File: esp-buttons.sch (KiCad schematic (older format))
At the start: 35 parts, among them Q1 FDV304P, U1 ESP-07v2, U2 LD1117S33CTR

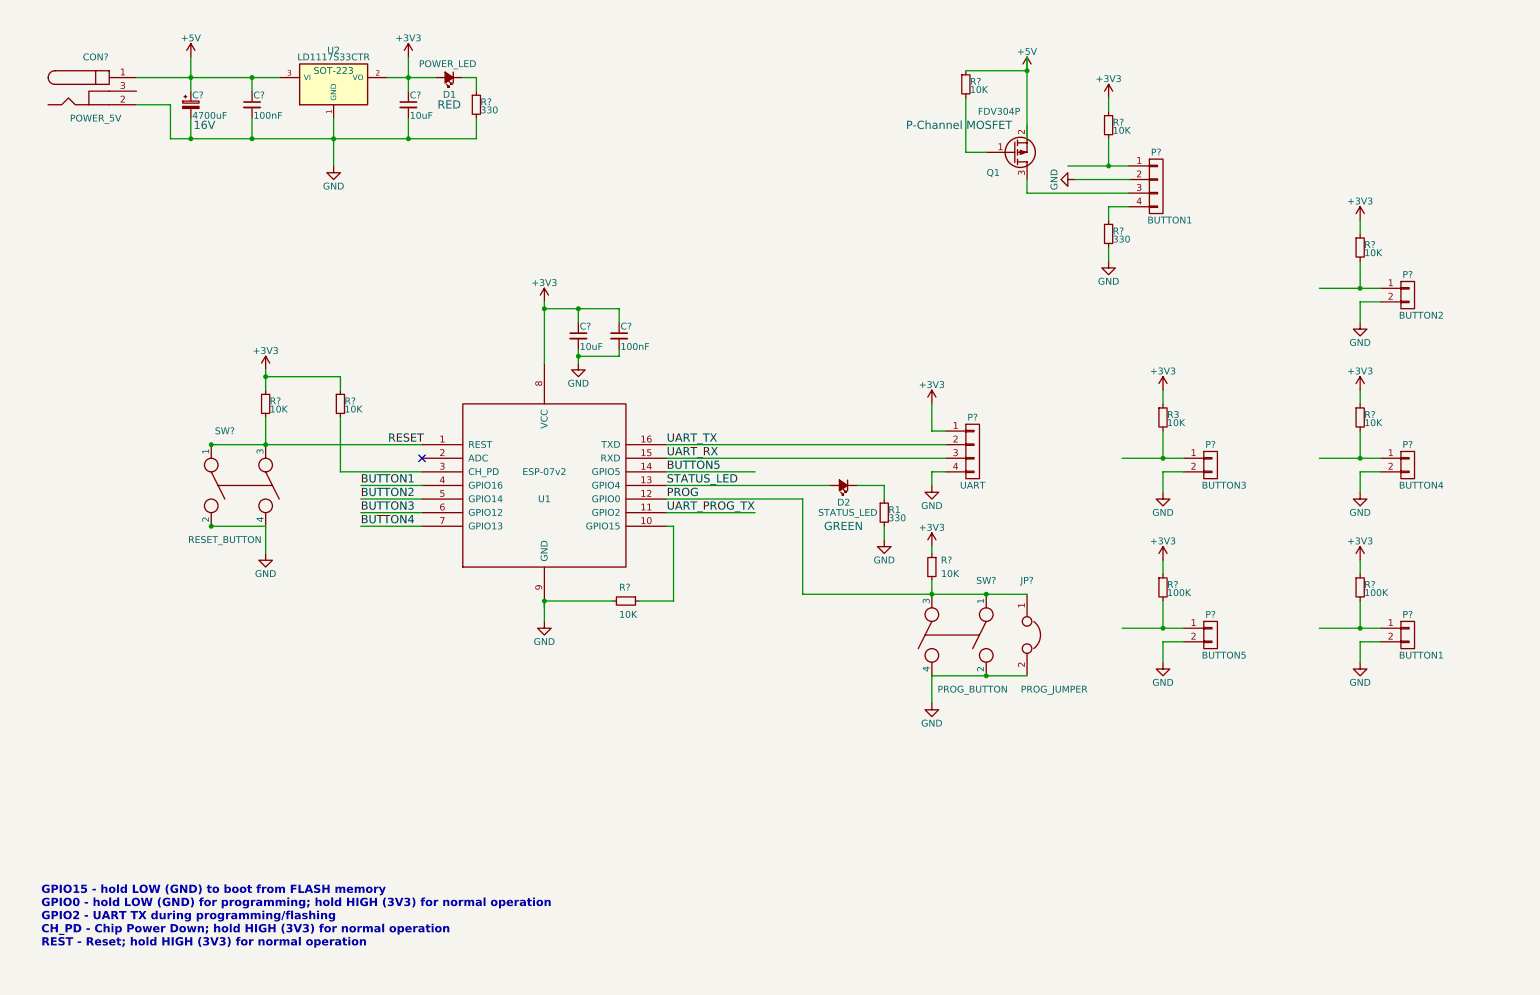
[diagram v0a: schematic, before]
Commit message: Removed one extra button circuitry
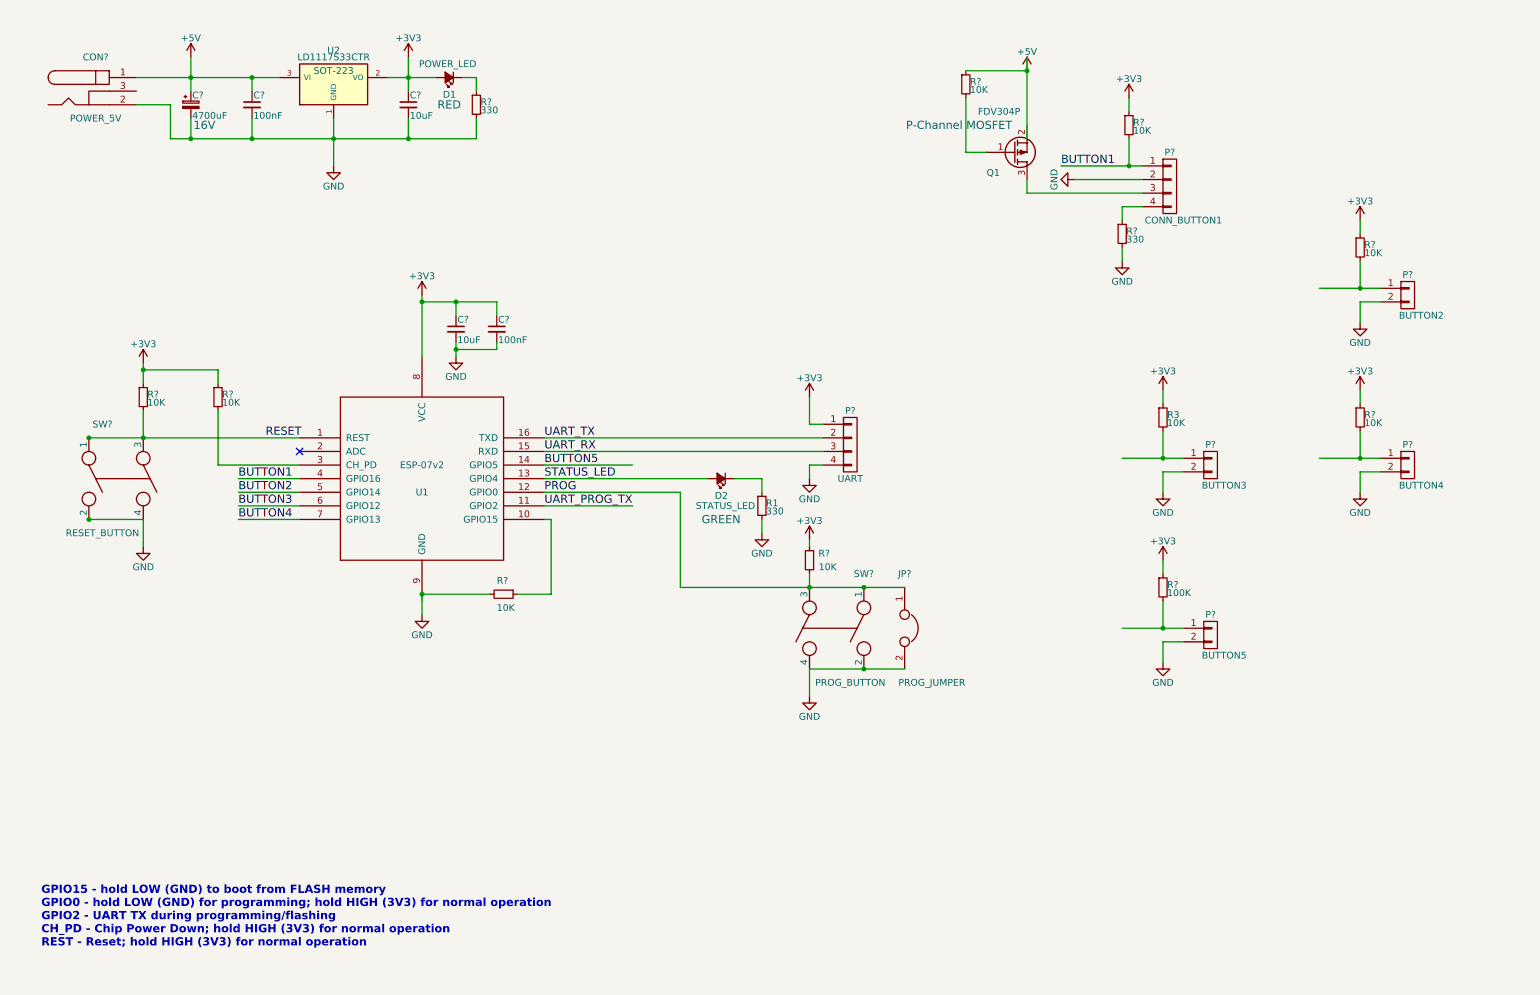
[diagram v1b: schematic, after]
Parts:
- removed P?: BUTTON1, symbol CONN_01X02
- removed R?: 100K, Resistors_SMD:R_1206_HandSoldering, symbol R_Small
- P?: value BUTTON1 -> CONN_BUTTON1
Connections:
- wire segments 98 -> 93
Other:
- moved on the sheet: C?, D2, JP?, P?, R1, R?, SW?, U1

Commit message: Minor modification to the POWER LED. Removed from repository the files that are in .gitignore
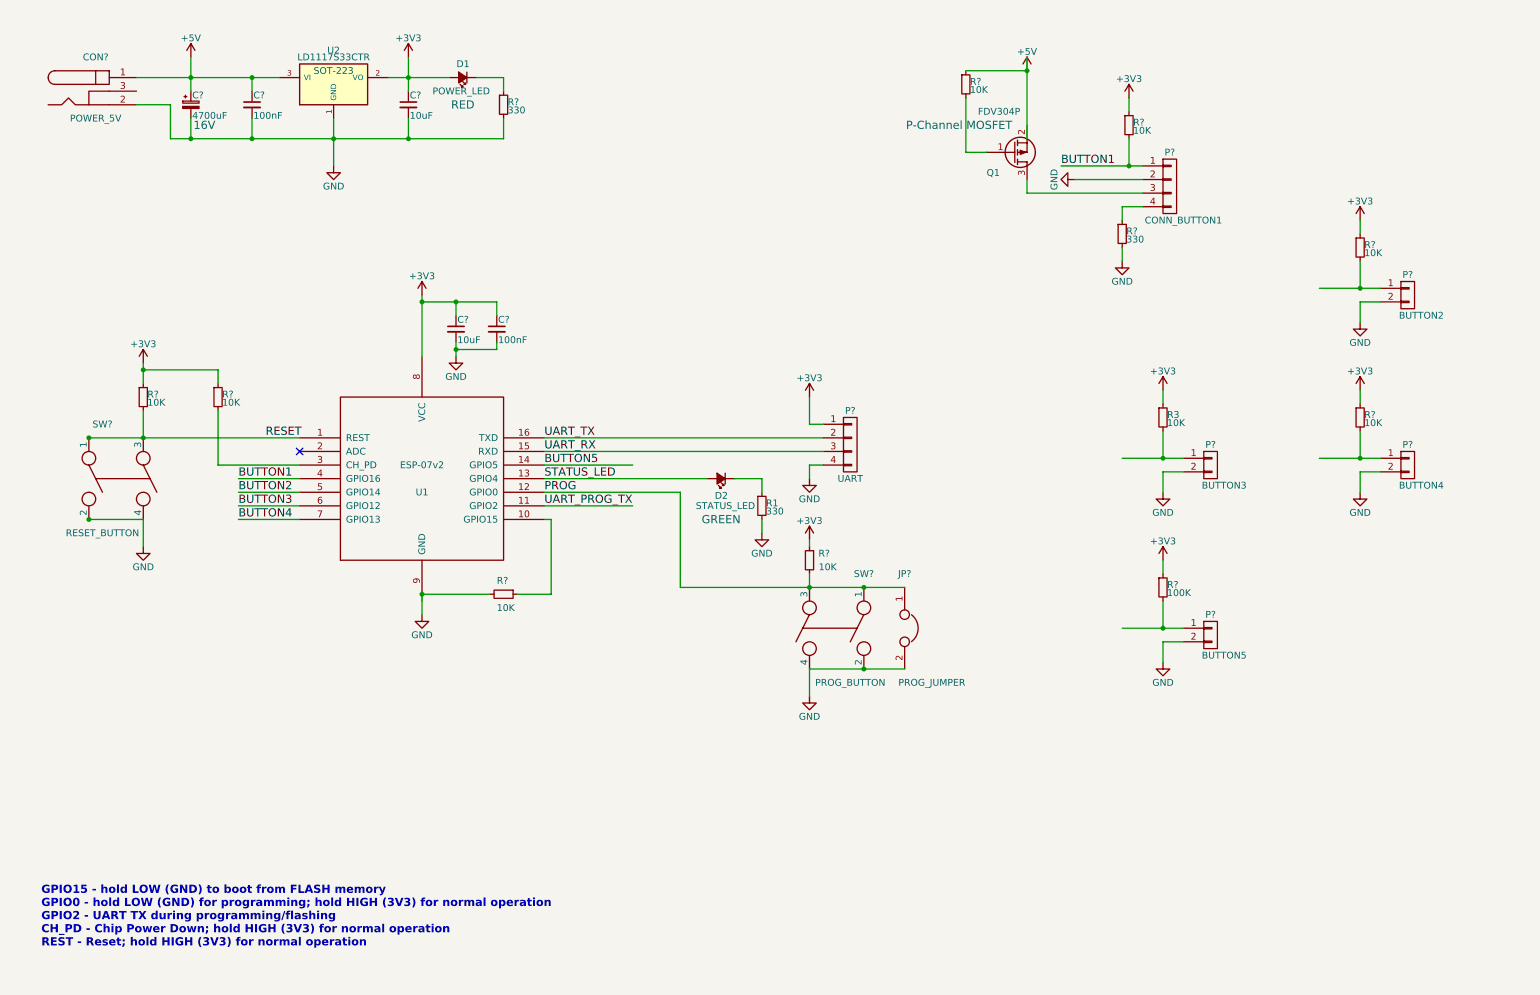
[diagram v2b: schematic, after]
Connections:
- wire segments 93 -> 117
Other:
- moved on the sheet: D1, R?
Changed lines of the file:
@@
 L Led_Small D1
 U 1 1 57C70C2A
-P 3700 1100
-F 0 "D1" H 3650 1225 50  0000 L CNN
-F 1 "POWER_LED" H 3500 1000 50  0000 L CNN
-F 2 "LEDs:LED_1206" V 3700 1100 50  0001 C CNN
-F 3 "" V 3700 1100 50  0000 C CNN
-F 4 "RED" H 3700 1300 60  0000 C CNN "Color"
-	1    3700 1100
+P 3800 1100
+F 0 "D1" H 3750 1000 50  0000 L CNN
+F 1 "POWER_LED" H 3600 1200 50  0000 L CNN
+F 2 "LEDs:LED_1206" V 3800 1100 50  0001 C CNN
+F 3 "" V 3800 1100 50  0000 C CNN
+F 4 "RED" H 3800 1300 60  0000 C CNN "Color"
+	1    3800 1100
 	-1   0    0    1
 $EndComp
@@
 L R_Small R?
 U 1 1 57C70C30
-P 3900 1300
-F 0 "R?" H 3930 1320 50  0000 L CNN
-F 1 "330" H 3930 1260 50  0000 L CNN
-F 2 "Resistors_SMD:R_1206_HandSoldering" H 3900 1300 50  0001 C CNN
-F 3 "" H 3900 1300 50  0000 C CNN
-	1    3900 1300
+P 4100 1300
+F 0 "R?" H 4130 1320 50  0000 L CNN
+F 1 "330" H 4130 1260 50  0000 L CNN
+F 2 "Resistors_SMD:R_1206_HandSoldering" H 4100 1300 50  0001 C CNN
+F 3 "" H 4100 1300 50  0000 C CNN
+	1    4100 1300
 	1    0    0    -1
 $EndComp
@@
 $EndComp
 Wire Wire Line
-	1400 1100 2450 1100
-Wire Wire Line
-	3250 1100 3600 1100
+	1400 1100 1800 1100
+Wire Wire Line
+	1800 1100 2250 1100
+Wire Wire Line
+	2250 1100 2450 1100
+Wire Wire Line
+	3250 1100 3400 1100
+Wire Wire Line
+	3400 1100 3700 1100
 Wire Wire Line
 	2250 1550 2250 1400
 Wire Wire Line
-	2850 1400 2850 1750
-Wire Wire Line
-	3500 2700 3500 3150
-Wire Wire Line
-	1800 950  1800 1200
+	2850 1400 2850 1550
+Wire Wire Line
+	2850 1550 2850 1750
+Wire Wire Line
+	3500 2700 3500 2750
+Wire Wire Line
+	3500 2750 3500 3150
+Wire Wire Line
+	1800 950  1800 1100
+Wire Wire Line
+	1800 1100 1800 1200
 Connection ~ 3500 2750
 Wire Wire Line
 	3750 3150 3750 3150
 Wire Wire Line
-	3400 950  3400 1200
+	3400 950  3400 1100
+Wire Wire Line
+	3400 1100 3400 1200
 Connection ~ 1800 1100
 Wire Wire Line
@@
 	3400 1550 3400 1400
 Wire Wire Line
-	1650 1550 3900 1550
+	1650 1550 1800 1550
+Wire Wire Line
+	1800 1550 2250 1550
+Wire Wire Line
+	2250 1550 2850 1550
+Wire Wire Line
+	2850 1550 3400 1550
+Wire Wire Line
+	3400 1550 4100 1550
 Connection ~ 2850 1550
 Wire Wire Line
@@
 	8700 1550 8700 1750
 Wire Wire Line
-	8200 1750 8800 1750
+	8200 1750 8700 1750
+Wire Wire Line
+	8700 1750 8800 1750
 Wire Wire Line
 	8700 1250 8700 1350
@@
 	6000 4050 6000 4150
 Wire Wire Line
-	3900 1550 3900 1400
+	4100 1550 4100 1400
 Connection ~ 3400 1550
 Wire Wire Line
 	10400 2450 10400 2650
 Wire Wire Line
-	10100 2650 10550 2650
+	10100 2650 10400 2650
+Wire Wire Line
+	10400 2650 10550 2650
 Wire Wire Line
 	10400 2150 10400 2250
@@
 	8950 3700 8950 3900
 Wire Wire Line
-	8650 3900 9100 3900
+	8650 3900 8950 3900
+Wire Wire Line
+	8950 3900 9100 3900
 Wire Wire Line
 	8950 3400 8950 3500
@@
 	10400 3700 10400 3900
 Wire Wire Line
-	10100 3900 10550 3900
+	10100 3900 10400 3900
+Wire Wire Line
+	10400 3900 10550 3900
 Wire Wire Line
 	10400 3400 10400 3500
@@
 	8950 4950 8950 5150
 Wire Wire Line
-	8650 5150 9100 5150
+	8650 5150 8950 5150
+Wire Wire Line
+	8950 5150 9100 5150
 Wire Wire Line
 	8950 4650 8950 4750
@@
 Connection ~ 8950 5150
 Wire Wire Line
-	1450 3200 1450 3350
+	1450 3200 1450 3250
+Wire Wire Line
+	1450 3250 1450 3350
 Wire Wire Line
 	1450 3750 1450 3550
@@
 Connection ~ 1050 4350
 Wire Wire Line
-	1050 3750 2600 3750
+	1050 3750 1450 3750
+Wire Wire Line
+	1450 3750 2600 3750
 Wire Wire Line
 	4400 4050 5600 4050
@@
 	6000 4350 6000 4450
 Wire Wire Line
-	3800 1100 3900 1100
-Wire Wire Line
-	3900 1100 3900 1200
-Wire Wire Line
-	7950 950  7950 1550
+	3900 1100 4100 1100
+Wire Wire Line
+	4100 1100 4100 1200
+Wire Wire Line
+	7950 950  7950 1050
+Wire Wire Line
+	7950 1050 7950 1550
 Wire Wire Line
 	7500 1250 7500 1650
@@
 	6350 4850 6350 4750
 Wire Wire Line
-	6350 5450 7050 5450
+	6350 5450 6750 5450
+Wire Wire Line
+	6750 5450 7050 5450
 Wire Wire Line
 	6350 5450 6350 5650
@@
 Connection ~ 6750 5450
 Wire Wire Line
-	5400 4850 7050 4850
+	5400 4850 6350 4850
+Wire Wire Line
+	6350 4850 6750 4850
+Wire Wire Line
+	6750 4850 7050 4850
 Wire Wire Line
 	5400 4850 5400 4150
@@
 	3750 2850 3750 2750
 Wire Wire Line
-	3500 2750 4050 2750
+	3500 2750 3750 2750
+Wire Wire Line
+	3750 2750 4050 2750
 $Comp
 L C_Small C?
@@
 Connection ~ 3750 2750
 Wire Wire Line
-	3750 3150 3750 3050
+	3750 3150 3750 3100
+Wire Wire Line
+	3750 3100 3750 3050
 Wire Wire Line
 	4050 3050 4050 3100
